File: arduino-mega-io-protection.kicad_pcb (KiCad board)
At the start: 4 copper layers, 150.1 x 72 mm, 207 parts, among them J101 CONN_01X02, J102 CONN_01X02, J103 CONN_01X02, J104 CONN_01X02, J105 CONN_01X02, J106 CONN_01X02, J107 CONN_01X02, J108 CONN_01X36, J109 CONN_01X10, J110 CONN_02X18, J111 CONN_01X08, J112 CONN_01X08, J113 CONN_01X08, J114 CONN_01X08, J115 CONN_01X08, J116 CONN_01X02, J117 CONN_01X02, J118 CONN_01X02, P301 J1B1211CCD, SW301 SW_Push, U201 MOCD217M, U202 MOCD217M, U203 MOCD217M, U204 MOCD217M, U205 MOCD217M, U206 MOCD217M, U209 MOCD217M, U210 MOCD217M, U211 MOCD217M, U212 MOCD217M, U213 MOCD217M, U214 MOCD217M, U215 MOCD217M, U216 MOCD217M, U217 MOCD217M, U218 MOCD217M, U219 MOCD217M, U220 MOCD217M, U221 MOCD217M, U222 MOCD217M, U223 MOCD217M, U224 MOCD217M, U225 MOCD217M, U301 W5500, Y301 25Mhz

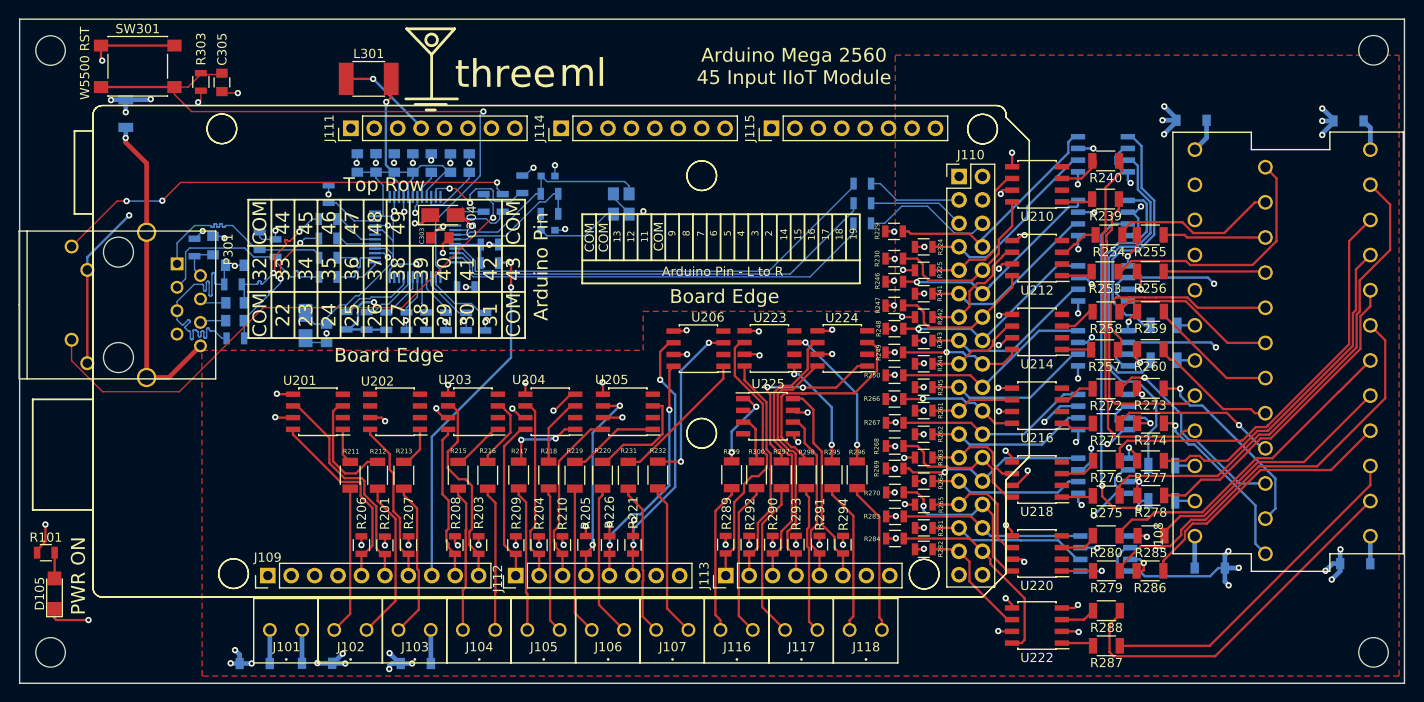
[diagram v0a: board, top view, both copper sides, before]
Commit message: updated for rev2 to go to OSHPark. Fixed footprints and changed topside routing to have better noise characteristics
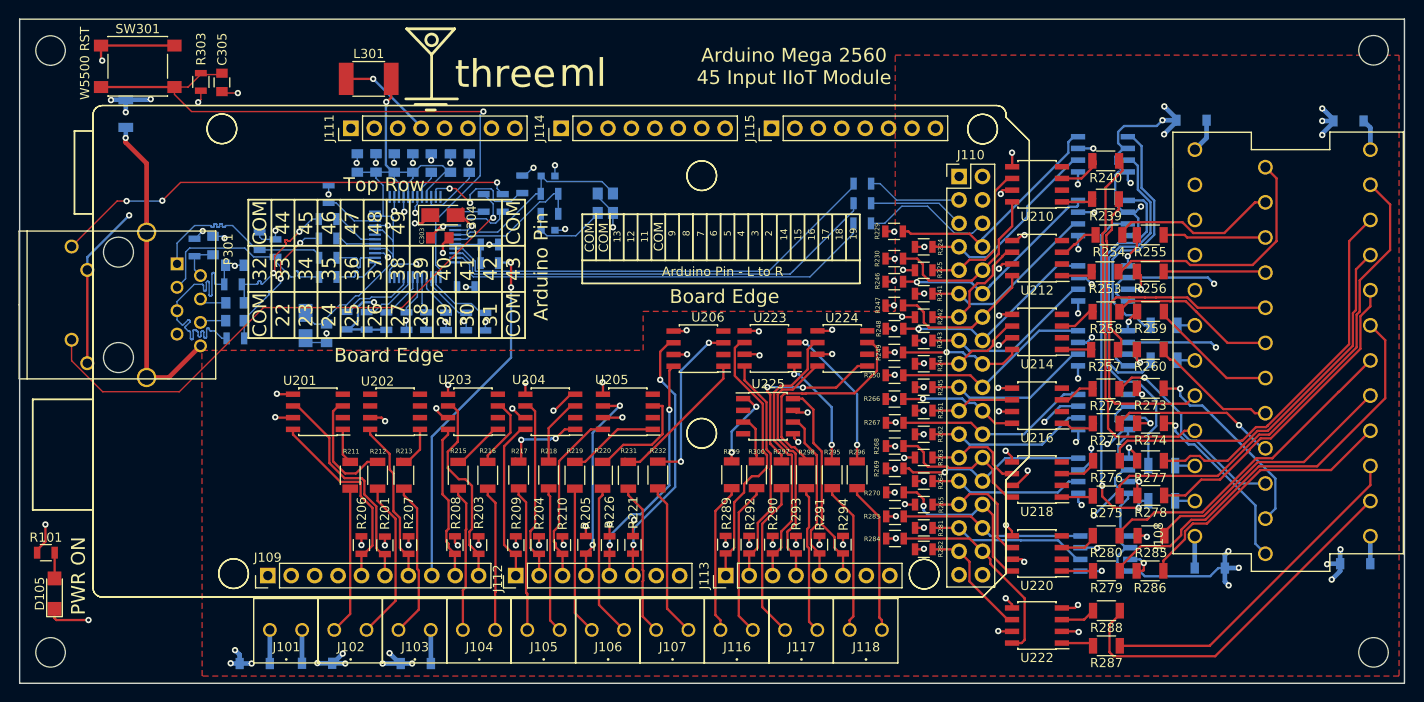
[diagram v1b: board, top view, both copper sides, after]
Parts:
- P301: footprint 3ML_W5500:J1B1211CCD -> 3ML_RJ45:J1B1211CCD
- Y301: footprint 3ML_SMD_Generic:3ML_4-SMD -> Oscillators:Oscillator_SMD_Abracon_ASE-4pin_3.2x2.5mm
- moved Y301 1.73 mm to (137.9, 93.8)
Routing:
- net GND: track 115.4 -> 141.0 mm
- net /W5500/XI/CLKN: track 23.9 -> 21.7 mm
- net Net-(C301-Pad1): track 10.9 -> 9.27 mm

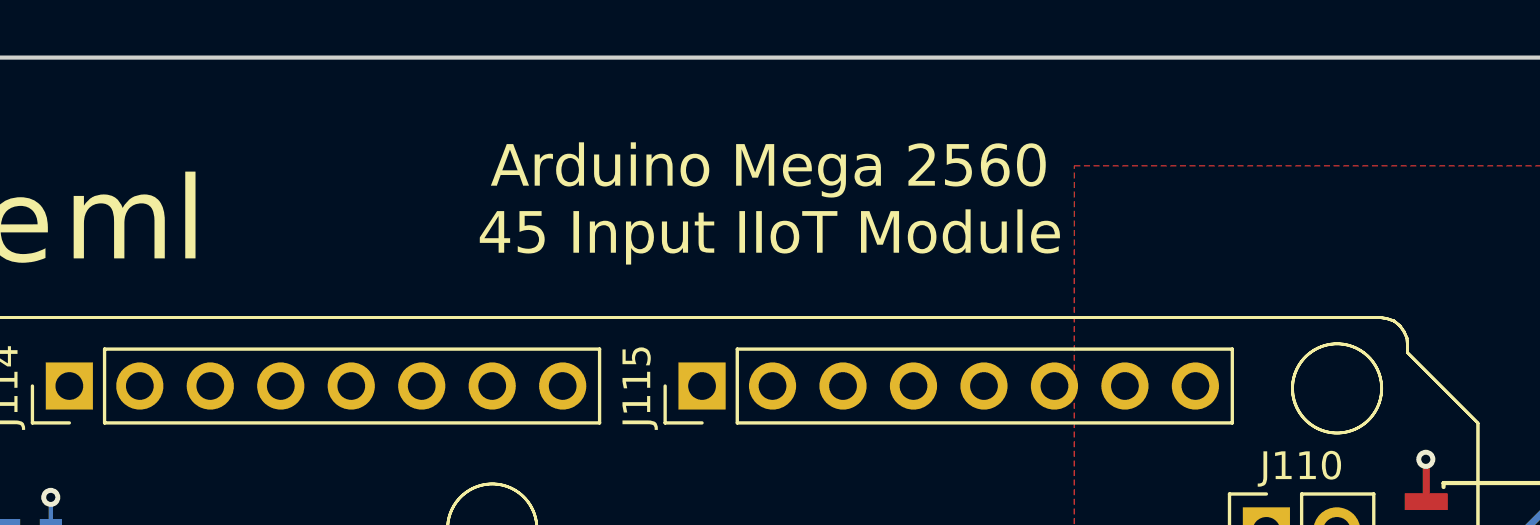
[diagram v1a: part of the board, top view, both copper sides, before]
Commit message: updating solder mask to reflect product name - sent to OSHPark
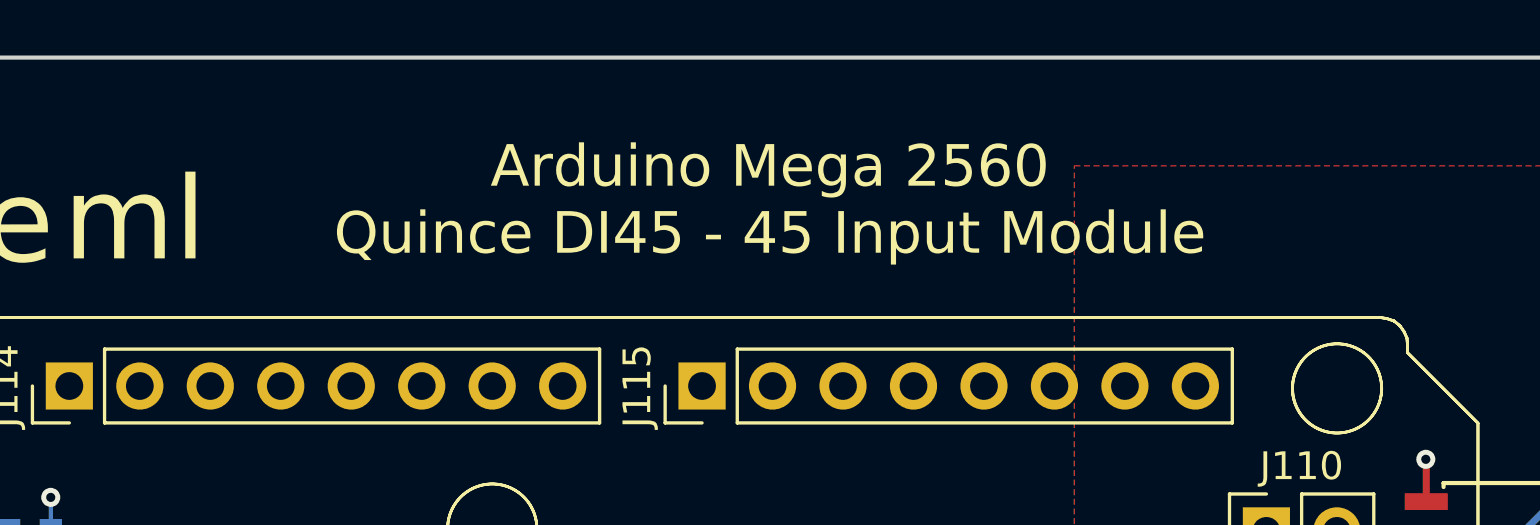
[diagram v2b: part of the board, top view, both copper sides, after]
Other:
- board text added: "Arduino Mega 2560 Quince DI45 - 45 Input Module"
- board text removed: "Arduino Mega 2560 45 Input IIoT Module"
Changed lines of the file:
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@@
     (links 458)
     (no_connects 0)
-    (area 74.372399 73.737399 224.661801 145.896401)
+    (area 35.253802 44.036001 230.290762 147.6956)
     (thickness 1.6)
     (drawings 119)
@@
     (35 F.Paste user)
     (36 B.SilkS user)
-    (37 F.SilkS user hide)
+    (37 F.SilkS user)
     (38 B.Mask user hide)
     (39 F.Mask user)
@@
     (effects (font (size 0.75 0.75) (thickness 0.1875)))
   )
-  (gr_text "Arduino Mega 2560\n45 Input IIoT Module" (at 158.4071 78.9432) (layer F.SilkS)
+  (gr_text "Arduino Mega 2560\nQuince DI45 - 45 Input Module" (at 158.4071 78.9432) (layer F.SilkS)
     (effects (font (size 1.5 1.5) (thickness 0.3)))
   )

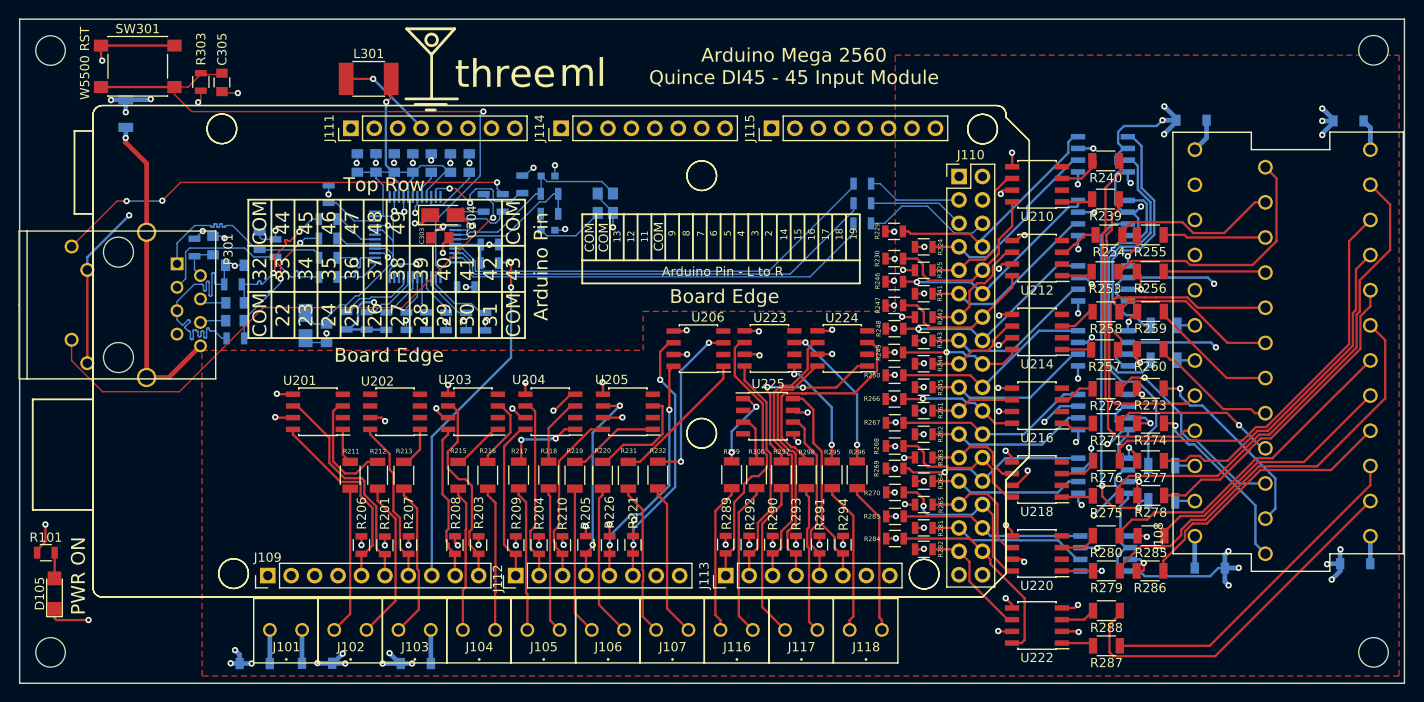
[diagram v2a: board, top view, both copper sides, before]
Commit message: moving diodes away from edge
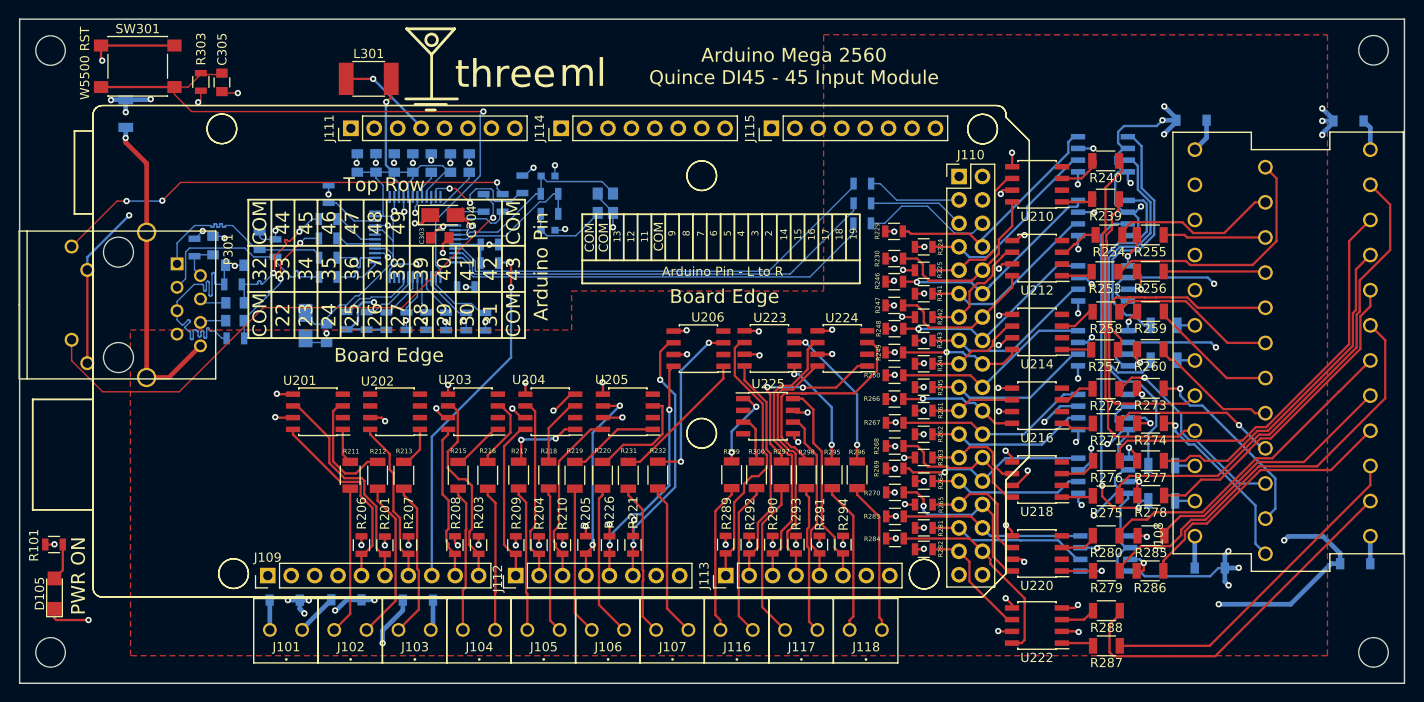
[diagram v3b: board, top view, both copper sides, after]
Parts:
- moved D101 7.61 mm to (103.2, 136.8), turned to 180 degrees
- moved D103 7.57 mm to (109.9, 136.8)
- moved D102 6.88 mm to (117.6, 136.8)
- moved R101 1.25 mm to (78.2, 130.8)
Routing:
- net GND: track 141.0 -> 160.0 mm, vias 30 -> 26
- net +5V: track 49.8 -> 47.4 mm
- net Net-(D105-Pad2): track 2.80 -> 4.07 mm
- net Net-(D103-Pad2): track 3.62 -> 4.58 mm

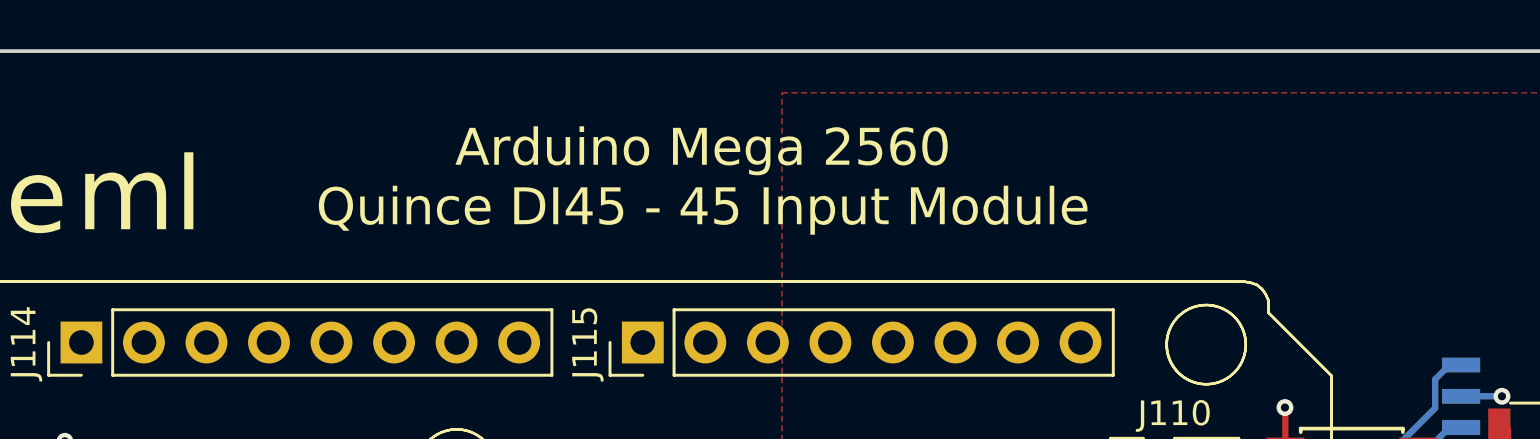
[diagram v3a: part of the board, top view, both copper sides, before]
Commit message: fixing diode location
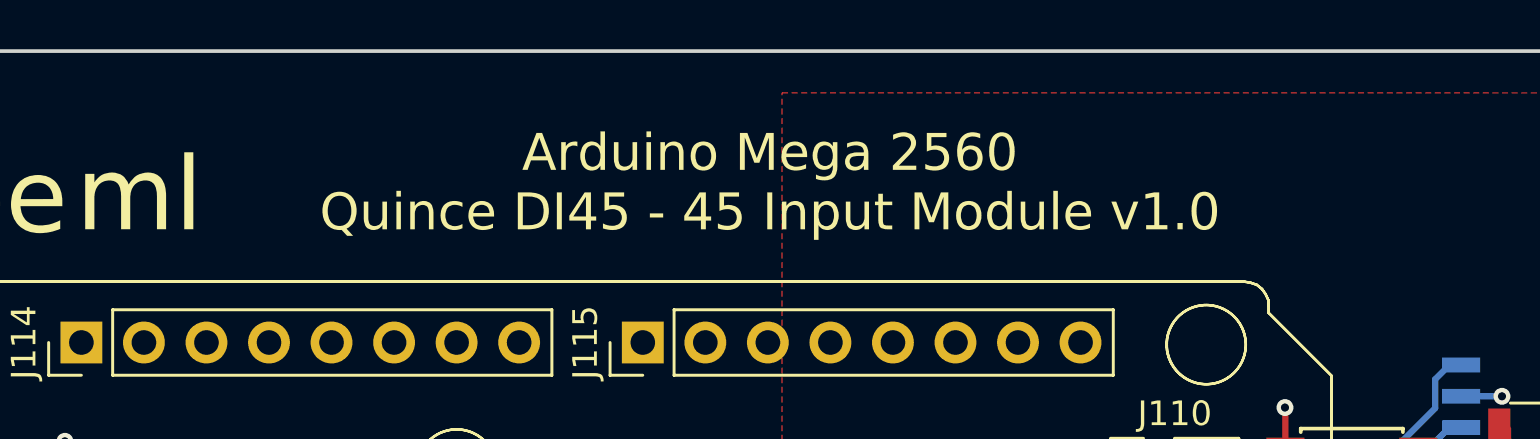
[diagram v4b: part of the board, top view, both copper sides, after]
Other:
- board text added: "Arduino Mega 2560 Quince DI45 - 45 Input Module v1.0"
- board text removed: "Arduino Mega 2560 Quince DI45 - 45 Input Module"
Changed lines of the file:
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@@
   (general
     (links 458)
-    (no_connects 1)
+    (no_connects 0)
     (area 35.253802 44.036001 230.290762 147.6956)
     (thickness 1.6)
@@
   )
   (setup
-    (last_trace_width 0.508)
+    (last_trace_width 0.152)
     (user_trace_width 0.1524)
     (user_trace_width 0.254)
@@
     (visible_elements 7FFFFF7F)
     (pcbplotparams
-      (layerselection 0x01000_00000000)
+      (layerselection 0x010fc_80000007)
       (usegerberextensions false)
       (excludeedgelayer true)
@@
       (drillshape 0)
       (scaleselection 1)
-      (outputdirectory "/Users/davisjp/Desktop/oshstencils - arduino-inputs/"))
+      (outputdirectory /Users/davisjp/Desktop/mf-quince/))
   )
   (net 0 "")
@@
     (effects (font (size 0.75 0.75) (thickness 0.1875)))
   )
-  (gr_text "Arduino Mega 2560\nQuince DI45 - 45 Input Module" (at 158.4071 78.9432) (layer F.SilkS)
+  (gr_text "Arduino Mega 2560\nQuince DI45 - 45 Input Module v1.0" (at 161.125 79.15) (layer F.SilkS)
     (effects (font (size 1.5 1.5) (thickness 0.3)))
   )
